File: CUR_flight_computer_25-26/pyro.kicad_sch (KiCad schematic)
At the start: 2 parts, among them U4 BUK9K25-40RAX, U5 BUK9K25-40RAX

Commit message: Implement RF reference design for LoRA module
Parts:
- removed U4, U5: BUK9K25-40RAX, BUK9K25-40RAX:BUK9K2540RAX, symbol BUK9K25-40RAX:BUK9K25-40RAX

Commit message: Update pyro.kicad_sch
just added the buk9k25 mosfet
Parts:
- added U4, U5: BUK9K25-40RAX, BUK9K25-40RAX:BUK9K2540RAX, symbol BUK9K25-40RAX:BUK9K25-40RAX

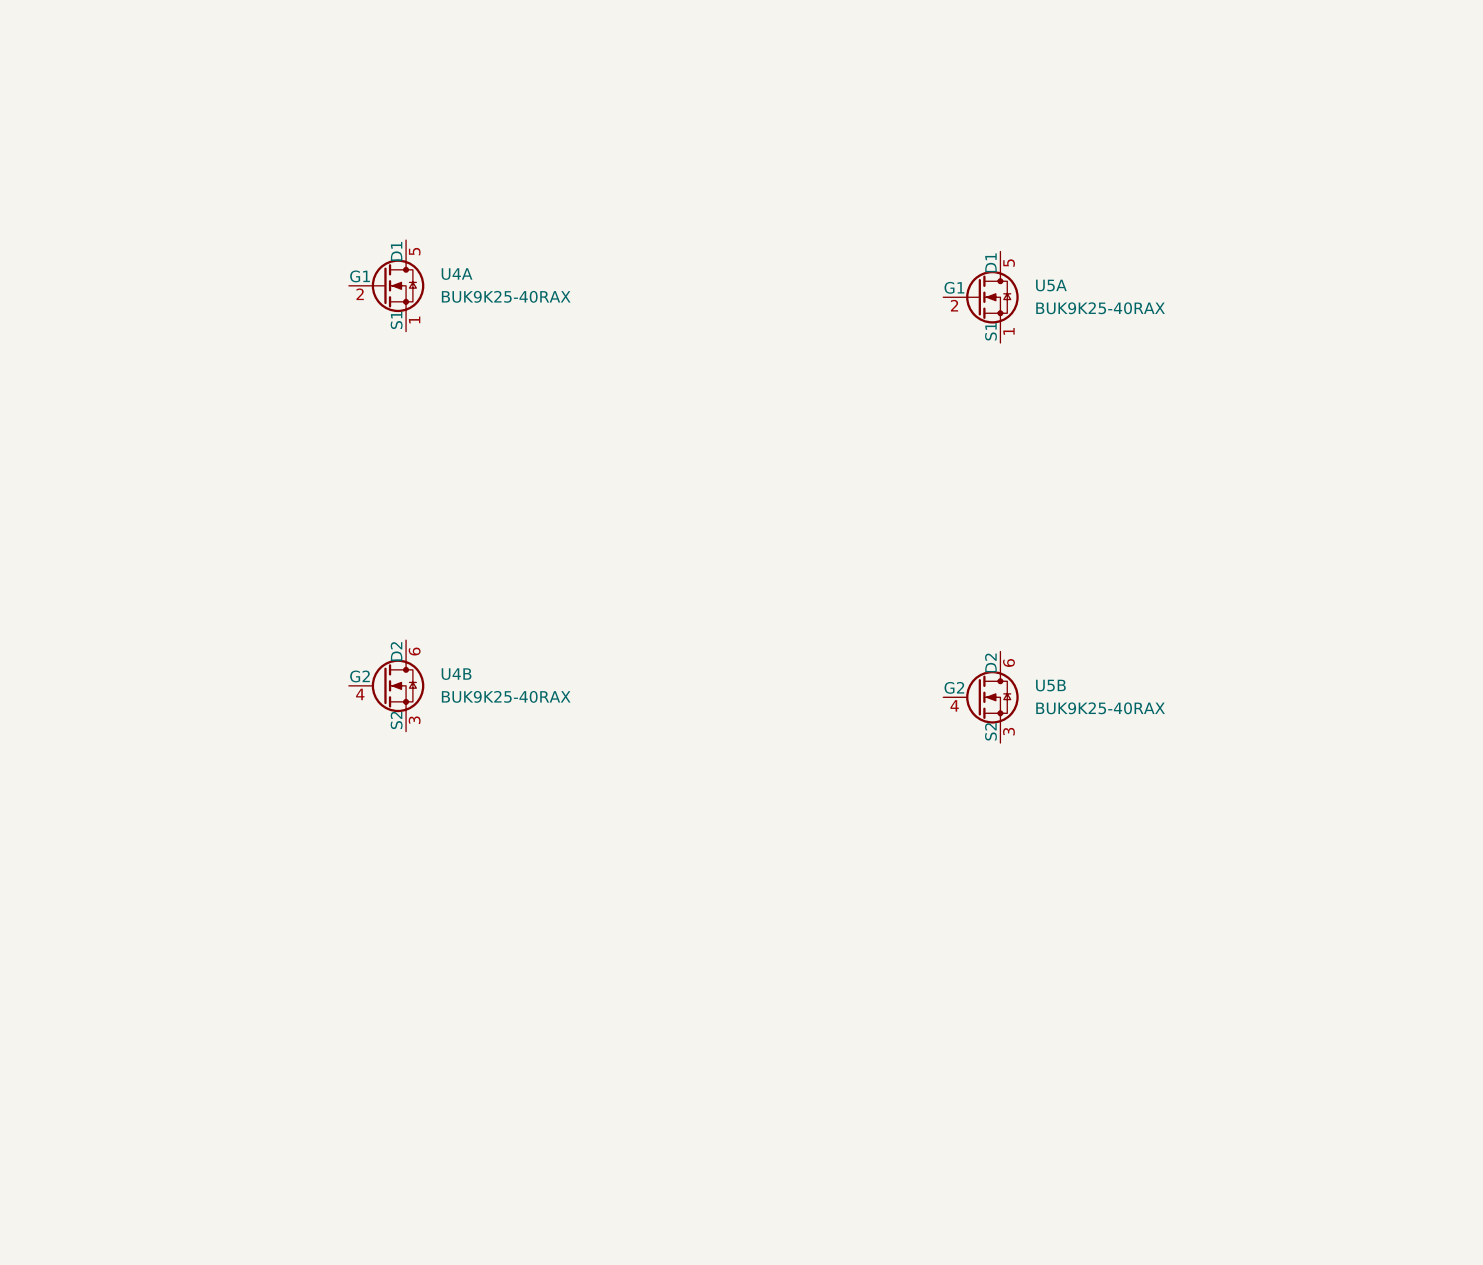
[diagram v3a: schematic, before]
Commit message: PYRO Channel
Set up PYRO channels 1-4
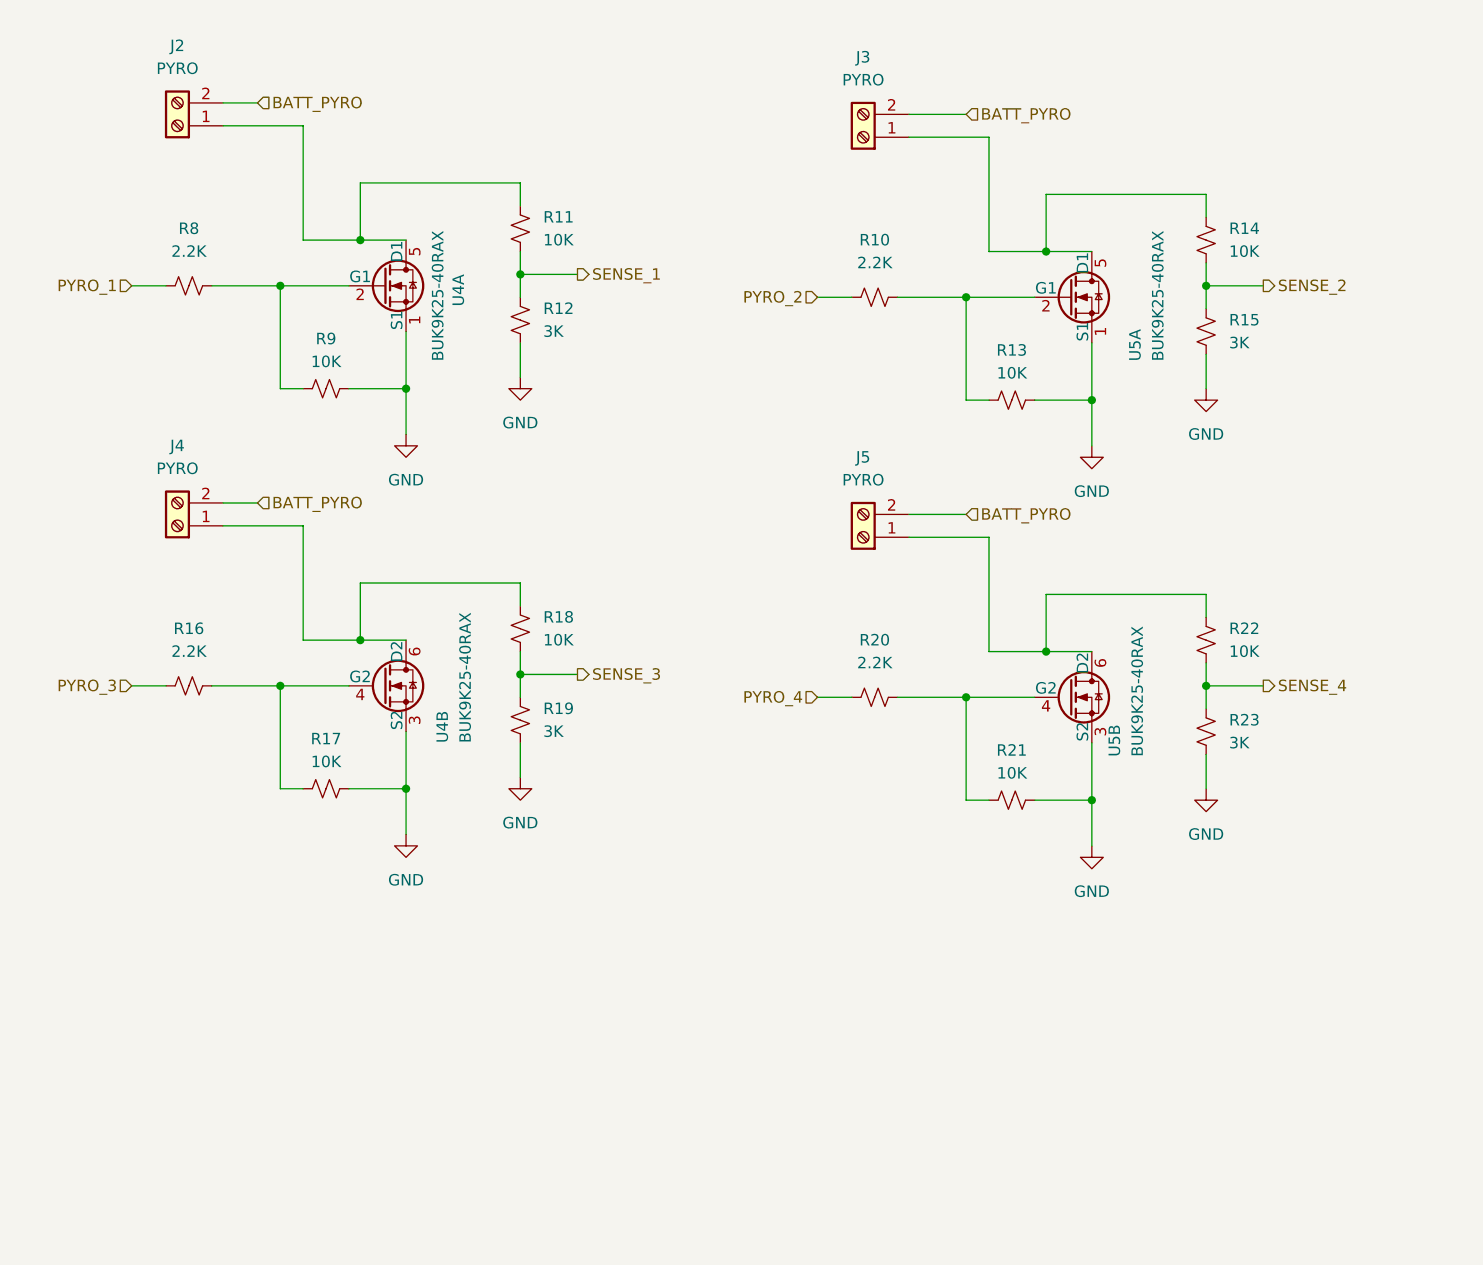
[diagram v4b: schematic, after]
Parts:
- added J2, J3, J4, J5: PYRO, symbol Connector:Screw_Terminal_01x02
- added R10, R16, R20, R8: 2.2K, symbol Device:R_Small_US
- added R11, R13, R14, R17, R18, R21, R22, R9: 10K, symbol Device:R_Small_US
- added R12, R15, R19, R23: 3K, symbol Device:R_Small_US
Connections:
- net GND: now reaches U4.3 (S2)
- net GND: now also U4.1 (S1), U5.1 (S1), U5.3 (S2), R12.2, R13.2, R15.2, R17.2, R19.2, R21.2, R23.2, R9.2
- net at U4.4 (G2): now also R16.2, R17.1
- net at U4.6 (D2): now also J4.1 (Pin_1), R18.1
- net at U4.2 (G1): now also R8.2, R9.1
- net at U4.5 (D1): now also J2.1 (Pin_1), R11.1
- net at U5.4 (G2): now also R20.2, R21.1
- net at U5.6 (D2): now also J5.1 (Pin_1), R22.1
- net at U5.2 (G1): now also R10.2, R13.1
- net at U5.5 (D1): now also J3.1 (Pin_1), R14.1
- new net BATT_PYRO: J2.2 (Pin_2), J3.2 (Pin_2), J4.2 (Pin_2), J5.2 (Pin_2)
- new net PYRO_1: R8.1
- new net PYRO_2: R10.1
- new net PYRO_3: R16.1
- new net PYRO_4: R20.1
- new net SENSE_1: R11.2, R12.1
- new net SENSE_2: R14.2, R15.1
- new net SENSE_3: R18.2, R19.1
- new net SENSE_4: R22.2, R23.1
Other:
- moved on the sheet: U5A, U5B

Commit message: updated pins
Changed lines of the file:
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@@
+		)
+	)
+	(global_label "BATT_PYRO"
+		(shape input)
+		(at 125.73 38.1 0)
+		(fields_autoplaced yes)
+		(effects
+			(font
+				(size 1.27 1.27)
+			)
+			(justify left)
+		)
+		(property "Intersheetrefs" "${INTERSHEET_REFS}"
+			(at 138.9357 38.1 0)
+			(effects
+				(font
+					(size 1.27 1.27)
+				)
+				(justify left)
+				(hide yes)
+			)
+		)
+	)
+	(global_label "BATT_PYRO"
+		(shape input)
+		(at 125.73 82.55 0)
+		(fields_autoplaced yes)
+		(effects
+			(font
+				(size 1.27 1.27)
+			)
+			(justify left)
+		)
+		(property "Intersheetrefs" "${INTERSHEET_REFS}"
+			(at 138.9357 82.55 0)
+			(effects
+				(font
+					(size 1.27 1.27)
+				)
+				(justify left)
+				(hide yes)
+			)
+		)
+	)
+	(global_label "BATT_PYRO"
+		(shape input)
+		(at 46.99 36.83 0)
+		(fields_autoplaced yes)
+		(effects
+			(font
+				(size 1.27 1.27)
+			)
+			(justify left)
+		)
+		(property "Intersheetrefs" "${INTERSHEET_REFS}"
+			(at 60.1957 36.83 0)
+			(effects
+				(font
+					(size 1.27 1.27)
+				)
+				(justify left)
+				(hide yes)
+			)
+		)
+	)
+	(global_label "BATT_PYRO"
+		(shape input)
+		(at 46.99 81.28 0)
+		(fields_autoplaced yes)
+		(effects
+			(font
+				(size 1.27 1.27)
+			)
+			(justify left)
+		)
+		(property "Intersheetrefs" "${INTERSHEET_REFS}"
+			(at 60.1957 81.28 0)
+			(effects
+				(font
+					(size 1.27 1.27)
+				)
+				(justify left)
+				(hide yes)
+			)
 		)
 	)
@@
 		)
 	)
-	(hierarchical_label "BATT_PYRO"
-		(shape input)
-		(at 125.73 82.55 0)
-		(effects
-			(font
-				(size 1.27 1.27)
-			)
-			(justify left)
-		)
-	)
-	(hierarchical_label "BATT_PYRO"
-		(shape input)
-		(at 125.73 38.1 0)
-		(effects
-			(font
-				(size 1.27 1.27)
-			)
-			(justify left)
-		)
-	)
 	(hierarchical_label "PYRO_1"
 		(shape input)
@@
 		)
 	)
-	(hierarchical_label "BATT_PYRO"
-		(shape input)
-		(at 46.99 81.28 0)
-		(effects
-			(font
-				(size 1.27 1.27)
-			)
-			(justify left)
-		)
-	)
-	(hierarchical_label "BATT_PYRO"
-		(shape input)
-		(at 46.99 36.83 0)
-		(effects
-			(font
-				(size 1.27 1.27)
-			)
-			(justify left)
-		)
-	)

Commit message: added dubugging
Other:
- note added: "Pyro Channels 1-4"
- moved on the sheet: J2, J3, J4, J5, R10, R11, R12, R13, R14, R15, R16, R17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

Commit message: updated all needed fixes
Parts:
- added D13, D14, D15, D16: ESDZV5HS-1BF4, symbol Device:D_TVS_Small
- renumbered J3 to J10, J5 to J11, J2 to J8, J4 to J9, R8 to R30, R16 to R31, R9 to R32, R17 to R33, R11 to R34, R12 to R35, R18 to R36, R19 to R37, R10 to R38, R20 to R39, R13 to R40, R21 to R41, R14 to R42, R15 to R43, R22 to R44, R23 to R45, U4 to U12, U5 to U13
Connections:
- net BATT_PYRO: now also D13.2 (A2), D14.2 (A2), D15.2 (A2), D16.2 (A2); no longer J10.2 (Pin_2), J11.2 (Pin_2), J8.2 (Pin_2), J9.2 (Pin_2)
- new net: D14.1 (A1), J9.2 (Pin_2)
- new net: D16.1 (A1), J10.2 (Pin_2)
- new net: D13.1 (A1), J8.2 (Pin_2)
- new net: D15.1 (A1), J11.2 (Pin_2)

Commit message: assigned footrpint
need to double check:
- HSE
- Capacitors

for some unknown reason cur kicad library refuses to work
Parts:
- D13, D14, D15, D16: footprint (none) -> Diode_SMD:D_0201_0603Metric
- J10, J11, J8, J9: footprint (none) -> TerminalBlock_Phoenix:TerminalBlock_Phoenix_PT-1,5-2-5.0-H_1x02_P5.00mm_Horizontal
- R30, R31, R32, R33, R34, R35, R36, R37, R38, R39, R40, R41, R42, R43, R44, R45: footprint (none) -> Resistor_SMD:R_0603_1608Metric
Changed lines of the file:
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@@
 			)
 		)
-		(property "Footprint" ""
+		(property "Footprint" "Resistor_SMD:R_0603_1608Metric"
 			(at 66.04 81.28 0)
 			(effects
@@
 			)
 		)
-		(property "Footprint" ""
+		(property "Footprint" "TerminalBlock_Phoenix:TerminalBlock_Phoenix_PT-1,5-2-5.0-H_1x02_P5.00mm_Horizontal"
 			(at 49.53 123.19 0)
 			(effects
@@
 			)
 		)
-		(property "Footprint" ""
+		(property "Footprint" "Resistor_SMD:R_0603_1608Metric"
 			(at 163.83 133.35 0)
 			(effects
@@
 			)
 		)
-		(property "Footprint" ""
+		(property "Footprint" "Diode_SMD:D_0201_0603Metric"
 			(at 139.7 50.8 0)
 			(effects
@@
 			)
 		)
-		(property "Footprint" ""
+		(property "Footprint" "Resistor_SMD:R_0603_1608Metric"
 			(at 87.63 63.5 0)
 			(effects
@@
 			)
 		)
-		(property "Footprint" ""
+		(property "Footprint" "Resistor_SMD:R_0603_1608Metric"
 			(at 87.63 134.62 0)
 			(effects
@@
 			)
 		)
-		(property "Footprint" ""
+		(property "Footprint" "Resistor_SMD:R_0603_1608Metric"
 			(at 87.63 144.78 0)
 			(effects
@@
 			)
 		)
-		(property "Footprint" ""
+		(property "Footprint" "Resistor_SMD:R_0603_1608Metric"
 			(at 127 139.7 0)
 			(effects
@@
 			)
 		)
-		(property "Footprint" ""
+		(property "Footprint" "Resistor_SMD:R_0603_1608Metric"
 			(at 163.83 74.93 0)
 			(effects
@@
 			)
 		)
-		(property "Footprint" ""
+		(property "Footprint" "Diode_SMD:D_0201_0603Metric"
 			(at 63.5 49.53 0)
 			(effects
@@
 			)
 		)
-		(property "Footprint" ""
+		(property "Footprint" "Resistor_SMD:R_0603_1608Metric"
 			(at 142.24 151.13 0)
 			(effects
@@
 			)
 		)
-		(property "Footprint" ""
+		(property "Footprint" "Resistor_SMD:R_0603_1608Metric"
 			(at 50.8 69.85 0)
 			(effects
@@
 			)
 		)
-		(property "Footprint" ""
+		(property "Footprint" "Resistor_SMD:R_0603_1608Metric"
 			(at 142.24 82.55 0)
 			(effects
@@
 			)
 		)
-		(property "Footprint" ""
+		(property "Footprint" "TerminalBlock_Phoenix:TerminalBlock_Phoenix_PT-1,5-2-5.0-H_1x02_P5.00mm_Horizontal"
 			(at 49.53 52.07 0)
 			(effects
@@
 			)
 		)
-		(property "Footprint" ""
+		(property "Footprint" "Diode_SMD:D_0201_0603Metric"
 			(at 138.43 119.38 0)
 			(effects
@@
 			)
 		)
-		(property "Footprint" ""
+		(property "Footprint" "Resistor_SMD:R_0603_1608Metric"
 			(at 127 71.12 0)
 			(effects
@@
 			)
 		)
-		(property "Footprint" ""
+		(property "Footprint" "TerminalBlock_Phoenix:TerminalBlock_Phoenix_PT-1,5-2-5.0-H_1x02_P5.00mm_Horizontal"
 			(at 125.73 121.92 0)
 			(effects
@@
 			)
 		)
-		(property "Footprint" ""
+		(property "Footprint" "Resistor_SMD:R_0603_1608Metric"
 			(at 163.83 64.77 0)
 			(effects
@@
 			)
 		)
-		(property "Footprint" ""
+		(property "Footprint" "Diode_SMD:D_0201_0603Metric"
 			(at 66.04 120.65 0)
 			(effects
@@
 			)
 		)
-		(property "Footprint" ""
+		(property "Footprint" "Resistor_SMD:R_0603_1608Metric"
 			(at 163.83 143.51 0)
 			(effects
@@
 			)
 		)
-		(property "Footprint" ""
+		(property "Footprint" "TerminalBlock_Phoenix:TerminalBlock_Phoenix_PT-1,5-2-5.0-H_1x02_P5.00mm_Horizontal"
 			(at 125.73 53.34 0)
 			(effects
@@
 			)
 		)
-		(property "Footprint" ""
+		(property "Footprint" "Resistor_SMD:R_0603_1608Metric"
 			(at 87.63 73.66 0)
 			(effects
@@
 			)
 		)
-		(property "Footprint" ""
+		(property "Footprint" "Resistor_SMD:R_0603_1608Metric"
 			(at 50.8 140.97 0)
 			(effects
@@
 			)
 		)
-		(property "Footprint" ""
+		(property "Footprint" "Resistor_SMD:R_0603_1608Metric"
 			(at 66.04 152.4 0)
 			(effects
